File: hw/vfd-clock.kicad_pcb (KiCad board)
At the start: 2 copper layers, 150 x 50 mm, 47 parts, among them CON1 BARREL_JACK_2, CON2 BARREL_JACK_2, M1 MountingHole_4-5mm, M2 MountingHole_4-5mm, P1 ST_LINK, P2 GPS, Q1 PNP, Q2 PNP, SW1 SET, SW2 UP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

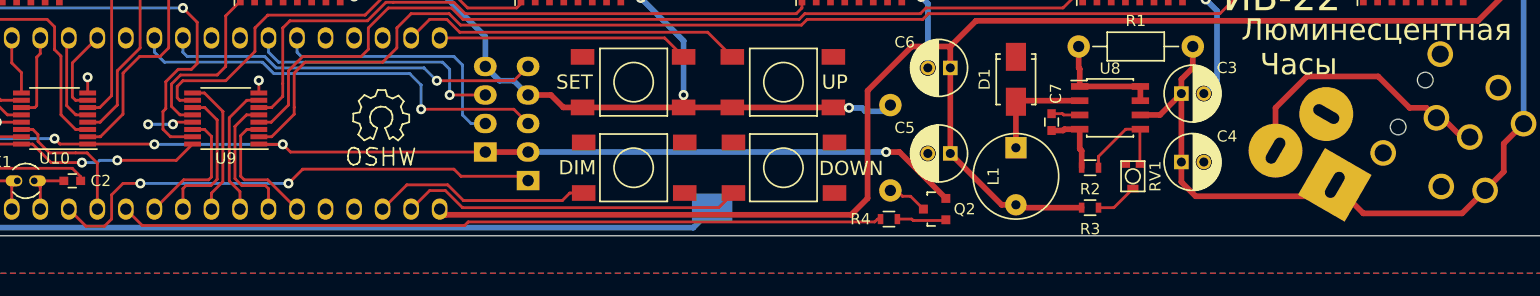
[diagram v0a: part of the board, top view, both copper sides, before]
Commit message: move grid/buz outputs to distinct PWM timer pins
rearrange a few traces for better ground fill and some silkscreen text
as well
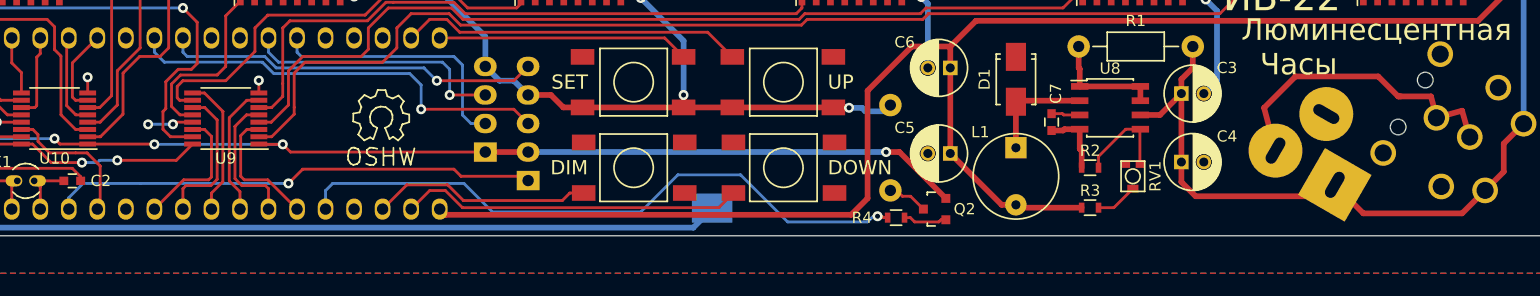
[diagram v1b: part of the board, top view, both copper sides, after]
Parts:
- moved R4 0.65 mm to (116.8, 73.8)
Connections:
- U1 pad 25: (no net) -> /BUZ
- U1 pad 32: /BUZ -> (no net)
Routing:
- net /BUZ: track 68.0 -> 56.4 mm, vias 0 -> 1
- net /GND: track 177.0 -> 180.9 mm
- net /RST: track 45.3 -> 43.4 mm, vias 2 -> 1
